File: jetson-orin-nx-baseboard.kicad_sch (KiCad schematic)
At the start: 0 parts

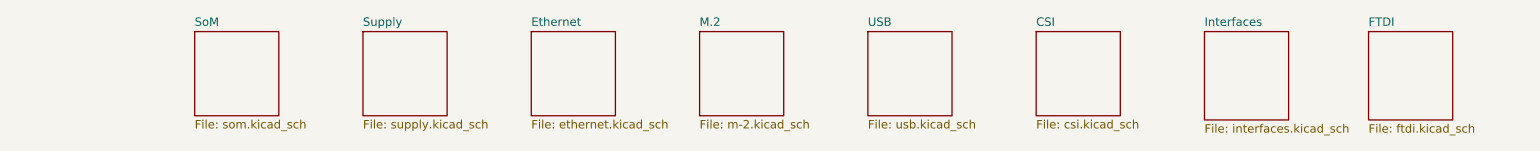
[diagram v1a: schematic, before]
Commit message: Schematic design for usb
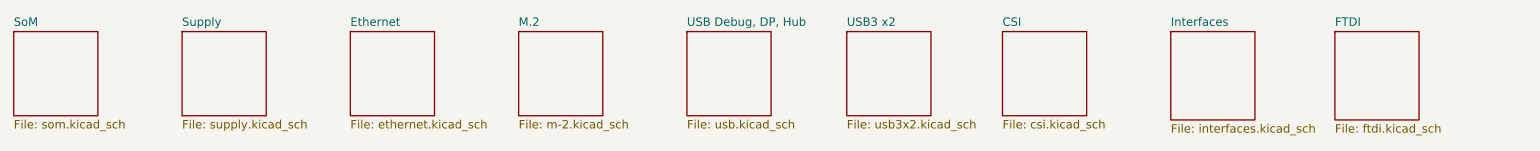
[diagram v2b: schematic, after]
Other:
- sheet USB renamed USB Debug, DP, Hub
- added sheet USB3 x2 (usb3x2.kicad_sch)

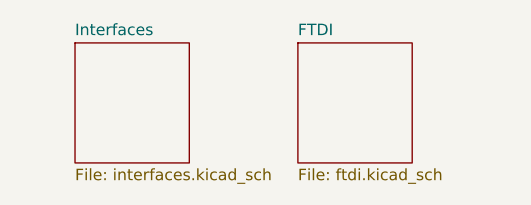
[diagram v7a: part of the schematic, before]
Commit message: Removed FTDI, added TPS65988 PD controller
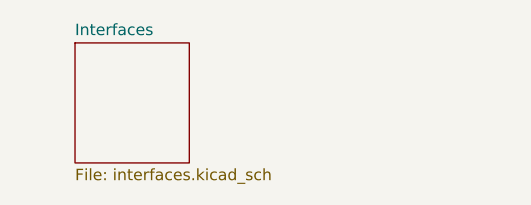
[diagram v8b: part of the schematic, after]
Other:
- removed sheet FTDI
